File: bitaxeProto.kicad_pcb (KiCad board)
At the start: 6 copper layers, 76 x 101 mm, 229 parts, among them J1 XT30, J4 Conn_01x04, J5 Conn_01x10, J6 USB_C_Receptacle_USB2.0, J8 TC2030-IDC, Q1 BSS138, SW3 SWITCH-SPST, SW4 SWITCH-SPST, U1 STHW4-DU-HN050206, U10 TLV77308PDBVR, U11 TLV77312PDBVR, U12 ESP32-S3-WROOM-1, U13 TS3011, U14 SN74AVC2T45DCUR, U15 25MHz, U19 TLV3542, U2 TPS546D24SRVFR, U4 TPS62933DRLR, U5 TPS62933DRLR, U6 TLV77312PDBVR, U7 TLV77308PDBVR, U8 25MHz, U9 TPS22919DCKR

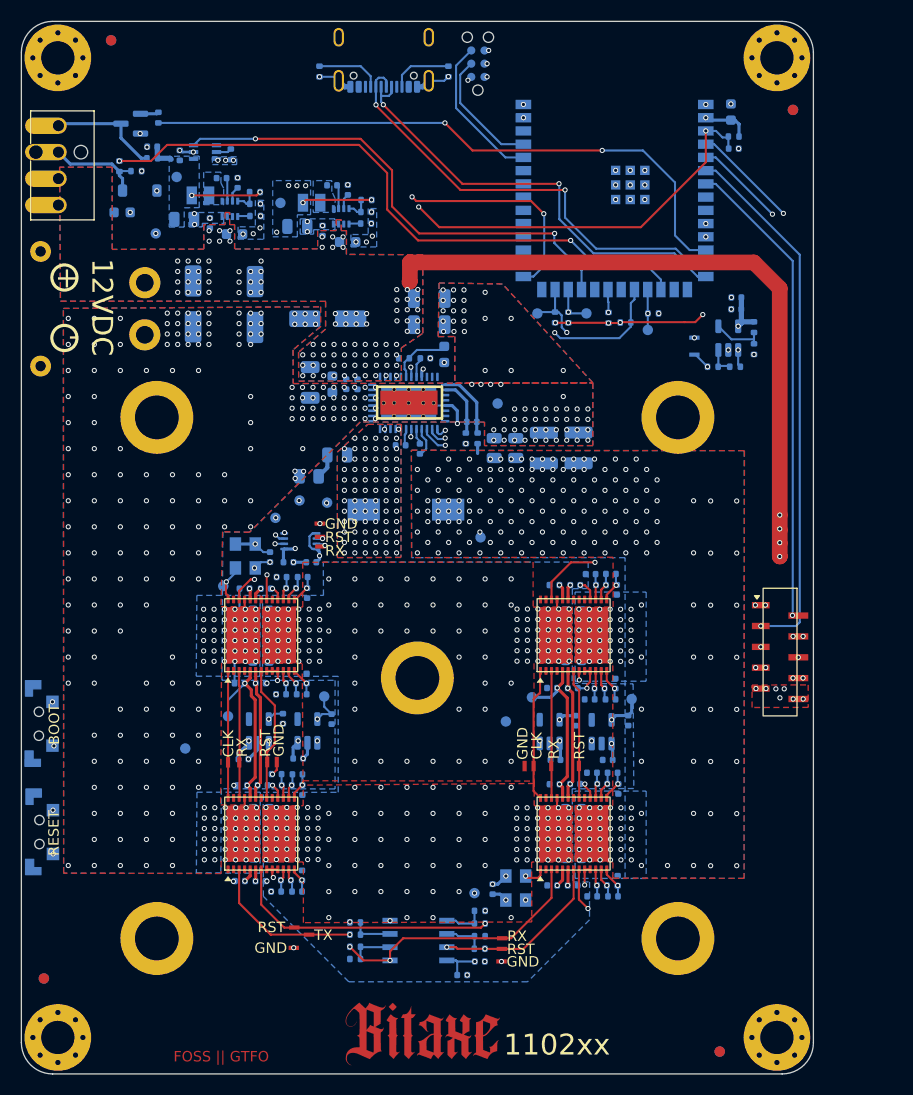
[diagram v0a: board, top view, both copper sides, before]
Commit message: fix TPS546 frequency for #4 - fix SN74AVC2T45 level shifter DIR voltage for #2
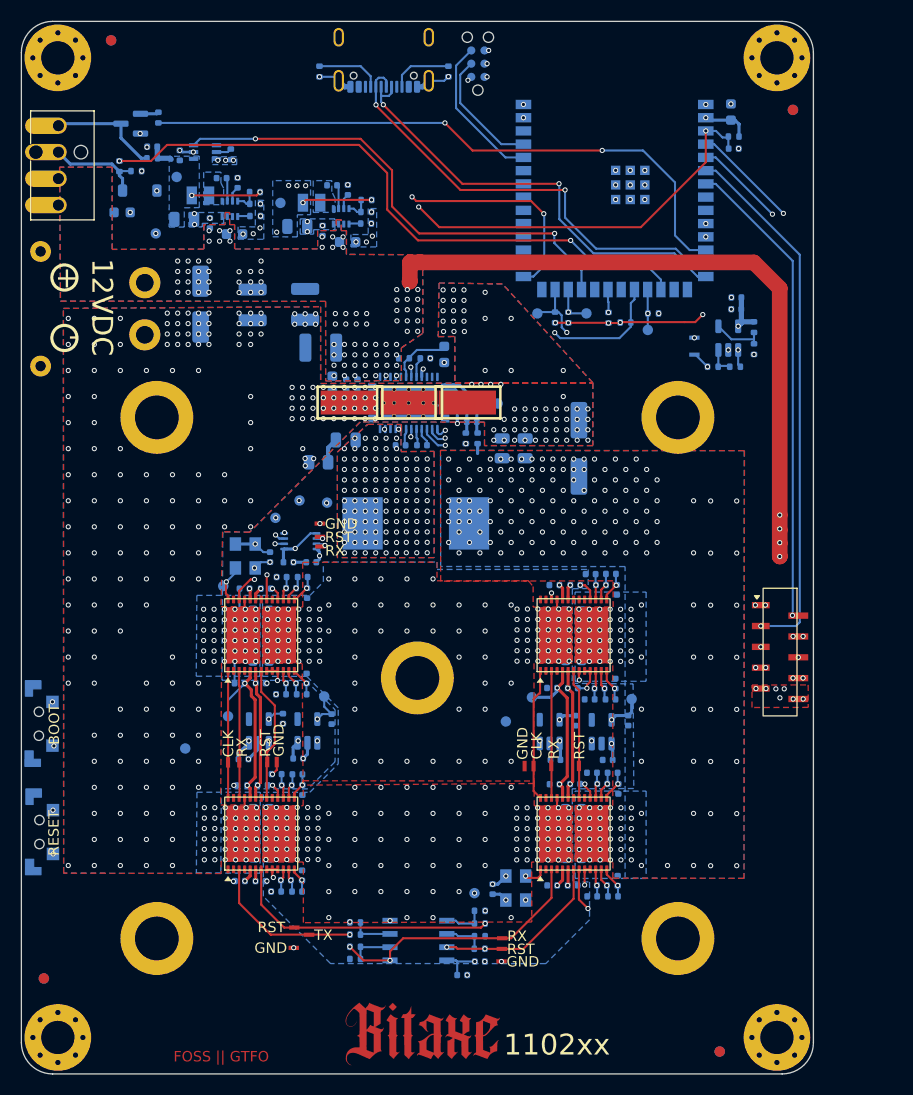
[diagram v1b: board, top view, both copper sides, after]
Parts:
- removed C1, C2: 68uF, Capacitor_SMD:CP_Elec_5x5.8
- removed C19, C6, C7: 4.7uF, Capacitor_SMD:C_1206_3216Metric
- removed C23, C24: 100uF, Capacitor_SMD:C_1210_3225Metric
- added C20: 10uF, Capacitor_SMD:C_1210_3225Metric, B.Cu at (121.7, 80.3)
- added C26: 10uF, Capacitor_SMD:C_1210_3225Metric, B.Cu at (120.2, 76.2)
- added C27: 10uF, Capacitor_SMD:C_1210_3225Metric, B.Cu at (115.2, 76.2)
- added C4: 330uF, Capacitor_SMD:CP_Elec_6.3x7.7, B.Cu at (146.5, 90.0)
- added U16: STHW4-DU-HN050206, bitaxe:PAD-SMD_L5.0-W2.0_STHW4-DU-HN050206, F.Cu at (124.5, 85.6)
- added U3: STHW4-DU-HN050206, bitaxe:PAD-SMD_L5.0-W2.0_STHW4-DU-HN050206, F.Cu at (135.8, 85.6)
- C21, C22: value 22uF -> 47uF
- C3: value 68uF -> 56uF; footprint Capacitor_SMD:CP_Elec_5x5.8 -> Capacitor_SMD:CP_Elec_5x5.3
- L1: value 230nH -> 320nH; footprint bitaxe:IND-SMD_L11.0-W7.2 -> bitaxe:IND_SLC1480_COC
- moved C3 12.3 mm to (110.2, 76.1), turned to -90 degrees
- moved C17 1.66 mm to (124.1, 89.2)
- moved R6 1.63 mm to (121.5, 91.3)
- moved L1 1.63 mm to (130.8, 97.2)
- moved C22 0.90 mm to (141.3, 90.0)
- moved C21 0.76 mm to (139.1, 90.0)
- moved C15 0.40 mm to (131.4, 89.7), turned to 180 degrees
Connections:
- U14 pad 5: /ASIC/1V2 -> /3V3
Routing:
- net /3V3: track 162.5 -> 165.1 mm
- net /ASIC/1V2: track 43.7 -> 41.2 mm
- net /Power/BP1v5: track 2.89 -> 1.76 mm
- net /VDD: vias 238 -> 221
- net /Power/SW1: vias 73 -> 103
- net /ASIC/GND0: vias 228 -> 225
- net /12V: vias 110 -> 99

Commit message: add domain voltage sensing for #3 -- just schematic so far
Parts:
- added C39: 0.1uF, Capacitor_SMD:C_0402_1005Metric, B.Cu at (175.8, 72.5)
- added C40: 0.1uF, Capacitor_SMD:C_0402_1005Metric, B.Cu at (175.8, 70.5)
- added R28: 5.1k, Resistor_SMD:R_0402_1005Metric, B.Cu at (172.9, 72.5)
- added R29: 5.1k, Resistor_SMD:R_0402_1005Metric, B.Cu at (172.9, 70.5)
- added R30: 10k, Resistor_SMD:R_0402_1005Metric, B.Cu at (172.9, 68.5)
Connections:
- U12 pad 15: unconnected-(U12-GPIO3/TOUCH3/ADC1_CH2*-Pad15) -> Net-(U12-GPIO3/TOUCH3/ADC1_CH2*)
- U12 pad 38: unconnected-(U12-GPIO2/TOUCH2/ADC1_CH1-Pad38) -> Net-(U12-GPIO2/TOUCH2/ADC1_CH1)

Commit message: update PCB to 1103x
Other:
- board text added: "1103x"
- board text removed: "1102xx"
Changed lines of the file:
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@@
 		(title "bitaxeProto")
 		(date "2026-05-12")
-		(rev "1102xx")
+		(rev "1103x")
 		(company "bitaxeorg")
 		(comment 1 "OHL v2")
@@
 		)
 	)
-	(gr_text "1102xx"
+	(gr_text "1103x"
 		(at 139.27 148.38 0)
 		(layer "F.SilkS")
